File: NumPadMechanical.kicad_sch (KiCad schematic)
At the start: 35 parts, among them SW1 Push_Button, SW10 Push_Button, SW11 Push_Button, SW12 Push_Button, SW13 Push_Button, SW14 Push_Button, SW15 Push_Button, SW16 Push_Button, SW17 Push_Button, SW2 Push_Button, SW3 Push_Button, SW4 Push_Button, SW5 Push_Button, SW6 Push_Button, SW7 Push_Button, SW8 Push_Button, SW9 Push_Button, U1 STM32F103C8Tx

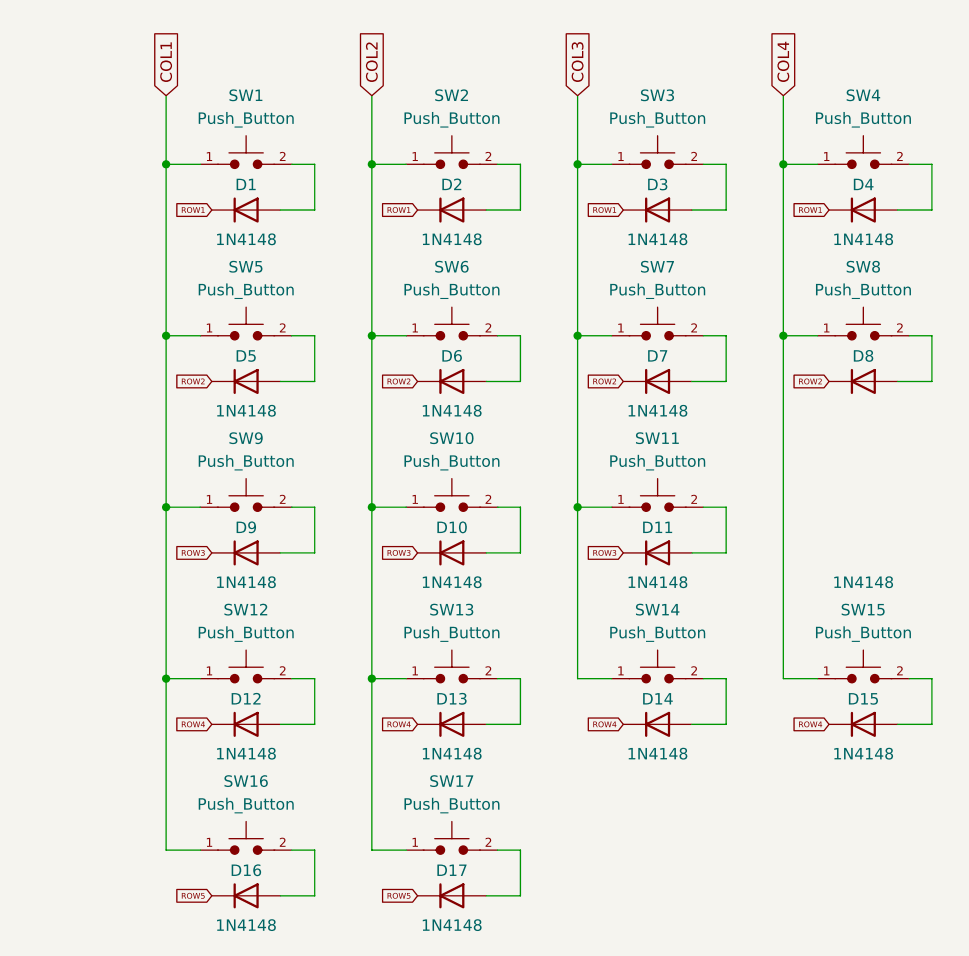
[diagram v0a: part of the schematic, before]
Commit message: Se agrega la matriz de switches al esquematico
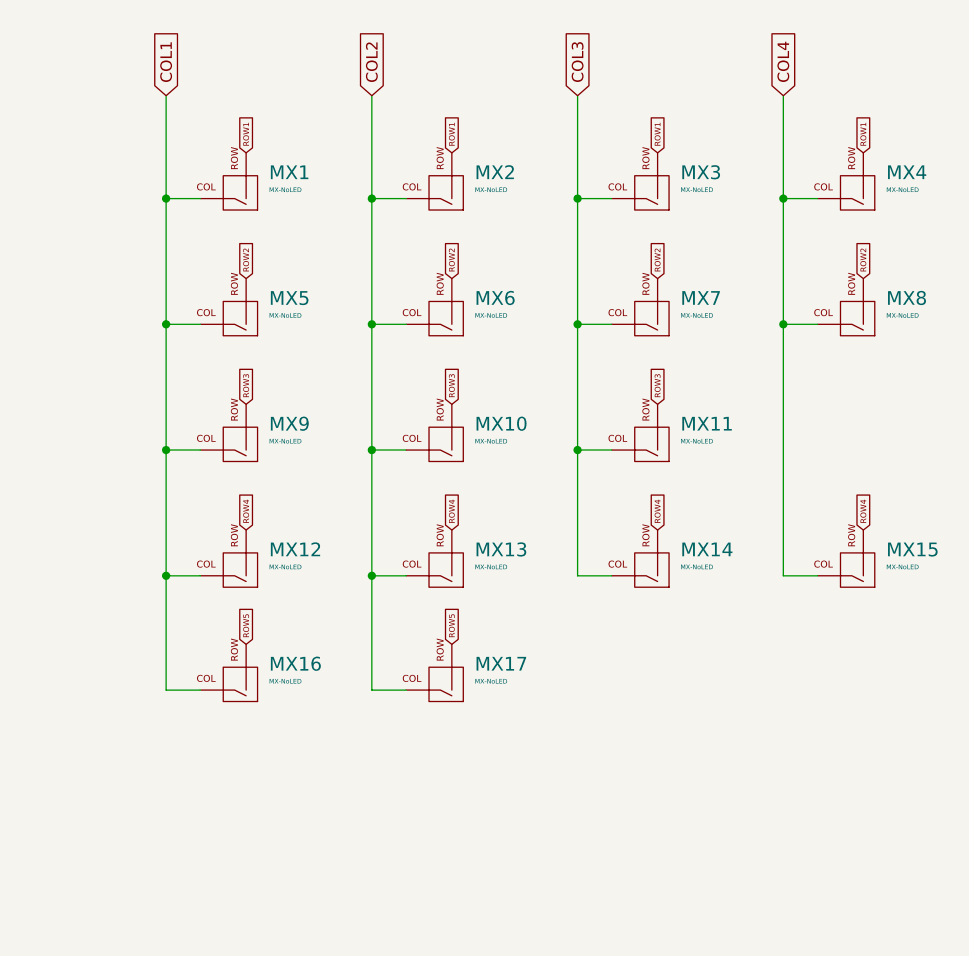
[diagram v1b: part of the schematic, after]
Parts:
- removed D1, D10, D11, D12, D13, D14, D15, D16, D17, D2, D3, D4, D5, D6, D7, D8, D9: 1N4148, Diode_THT:D_DO-35_SOD27_P7.62mm_Horizontal, symbol Diode:1N4148
- removed SW1, SW10, SW11, SW12, SW13, SW14, SW15, SW16, SW17, SW2, SW3, SW4, SW5, SW6, SW7, SW8, SW9: Push_Button, Button_Switch_THT:SW_PUSH_6mm, symbol PCM_SL_Devices:Push_Button
- added MX1, MX10, MX11, MX12, MX13, MX14, MX15, MX16, MX17, MX2, MX3, MX4, MX5, MX6, MX7, MX8, MX9: MX-NoLED, symbol MX_Alps_Hybrid:MX-NoLED
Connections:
- net COL1: now also MX1.1 (COL), MX12.1 (COL), MX16.1 (COL), MX5.1 (COL), MX9.1 (COL)
- net COL2: now also MX10.1 (COL), MX13.1 (COL), MX17.1 (COL), MX2.1 (COL), MX6.1 (COL)
- net COL3: now also MX11.1 (COL), MX14.1 (COL), MX3.1 (COL), MX7.1 (COL)
- net COL4: now also MX15.1 (COL), MX4.1 (COL), MX8.1 (COL)
- net ROW1: now also MX1.2 (ROW), MX2.2 (ROW), MX3.2 (ROW), MX4.2 (ROW)
- net ROW2: now also MX5.2 (ROW), MX6.2 (ROW), MX7.2 (ROW), MX8.2 (ROW)
- net ROW3: now also MX10.2 (ROW), MX11.2 (ROW), MX9.2 (ROW)
- net ROW4: now also MX12.2 (ROW), MX13.2 (ROW), MX14.2 (ROW), MX15.2 (ROW)
- net ROW5: now also MX16.2 (ROW), MX17.2 (ROW)

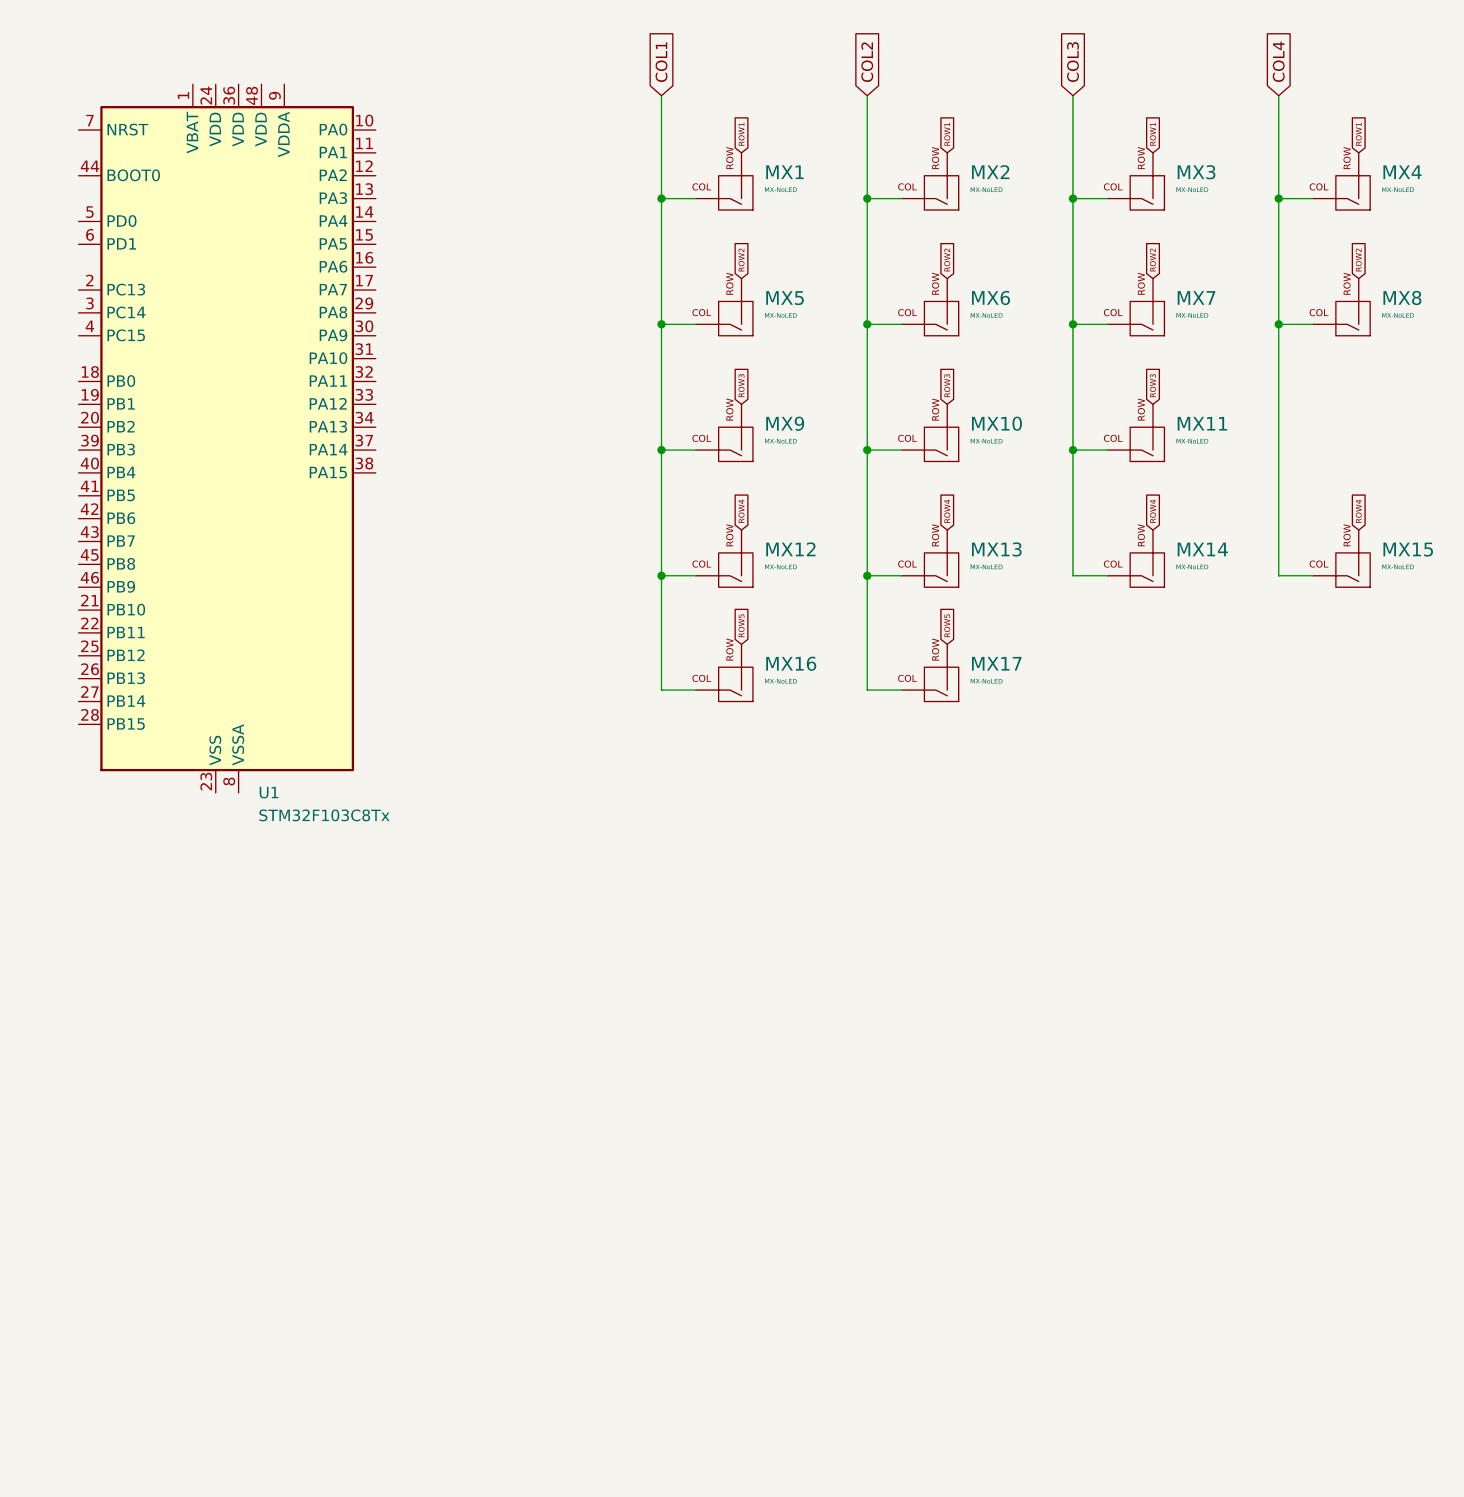
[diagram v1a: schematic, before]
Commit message: Se añaden diodos a la matriz de switches, se agrega conector usb y se coloca su cableado
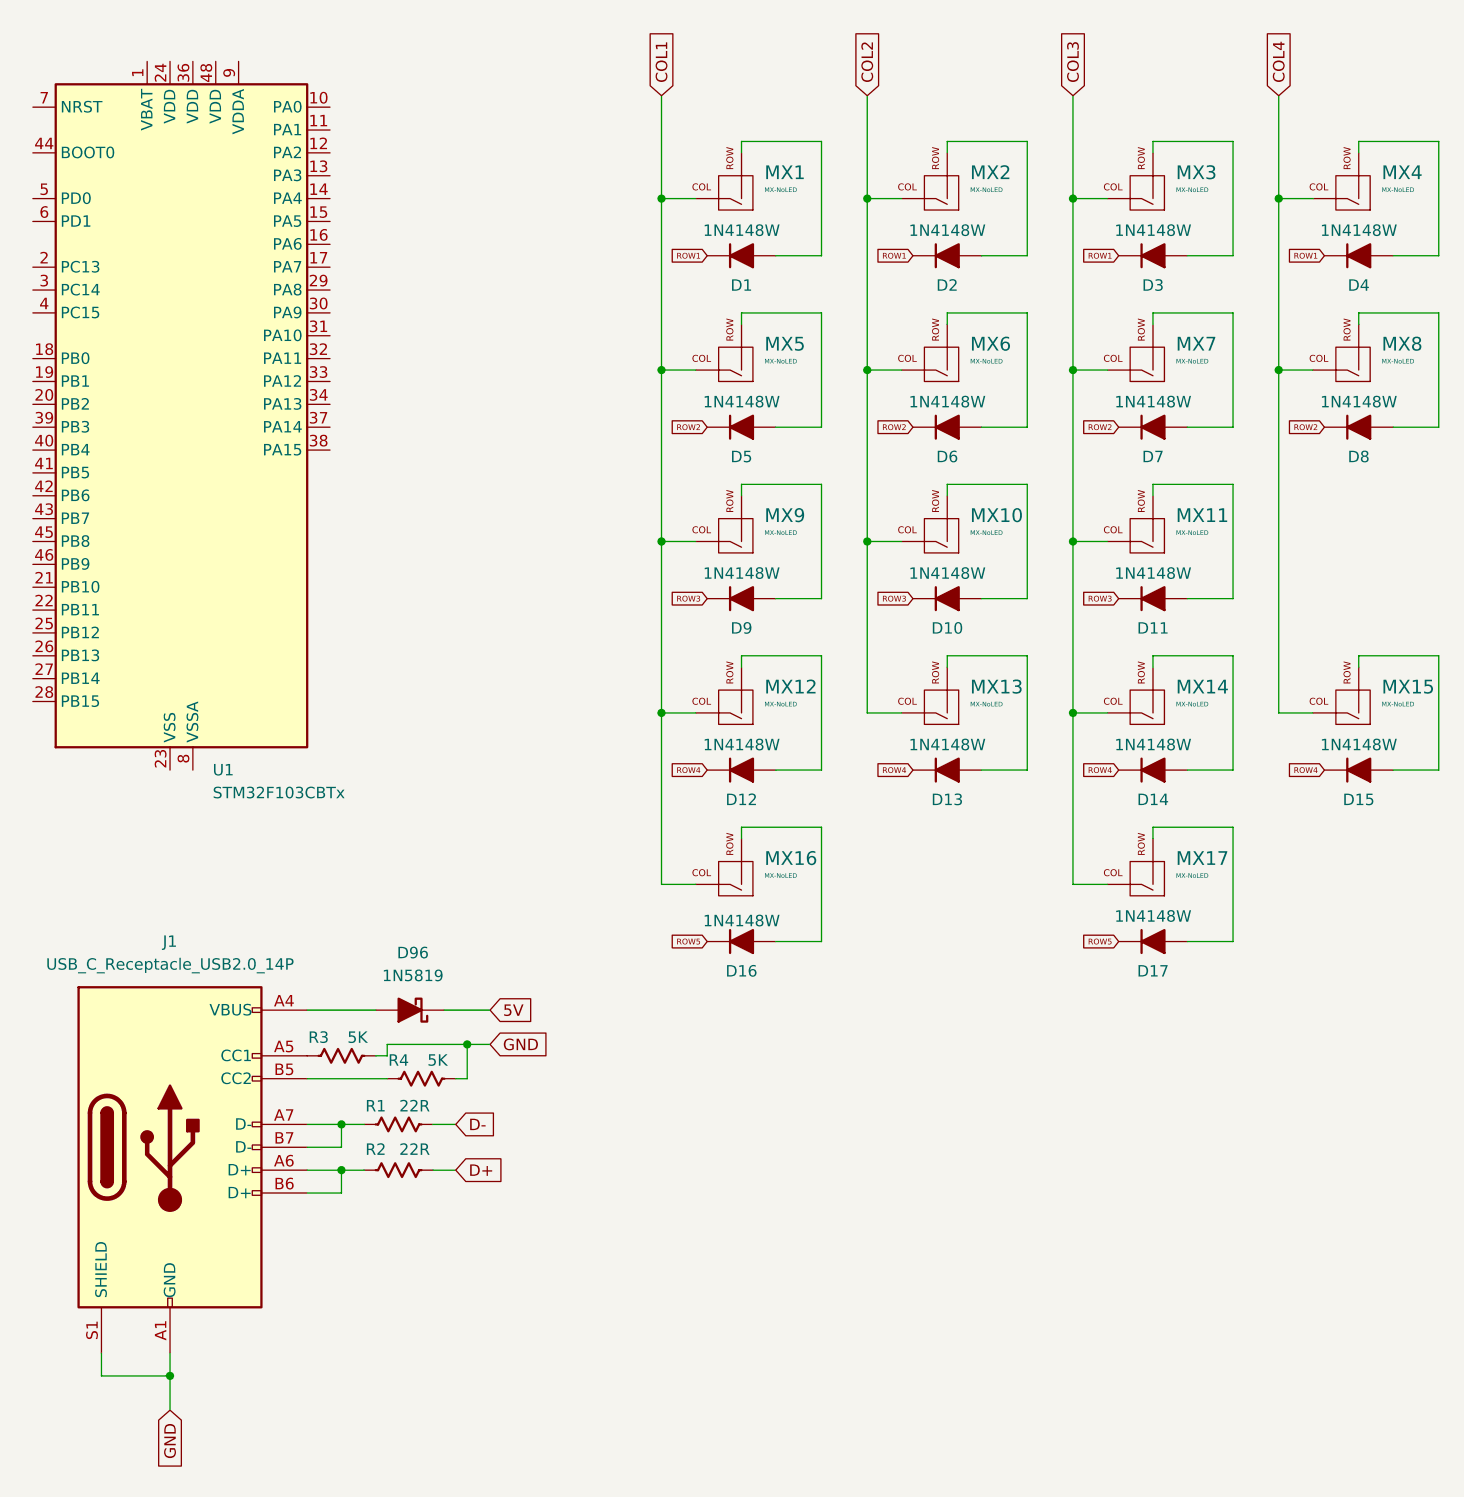
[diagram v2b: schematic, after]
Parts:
- removed U1: STM32F103C8Tx, Package_QFP:LQFP-48_7x7mm_P0.5mm, symbol MCU_ST_STM32F1:STM32F103C8Tx
- added D1, D10, D11, D12, D13, D14, D15, D16, D17, D2, D3, D4, D5, D6, D7, D8, D9: 1N4148W, Diode_SMD:D_SOD-123, symbol PCM_Diode_AKL:1N4148W
- added D96: 1N5819, Diode_SMD:D_SOD-123, symbol PCM_Diode_Schottky_AKL:D_Schottky_Generic
- added J1: USB_C_Receptacle_USB2.0_14P, Connector_USB:USB_C_Receptacle_XKB_U262-16XN-4BVC11, symbol Connector:USB_C_Receptacle_USB2.0_14P
- added R1, R2: 22R, Resistor_SMD:R_0603_1608Metric_Pad0.98x0.95mm_HandSolder, symbol PCM_Resistor_US_AKL:R_0603
- added R3, R4: 5K, Resistor_SMD:R_0603_1608Metric_Pad0.98x0.95mm_HandSolder, symbol PCM_Resistor_US_AKL:R_0603
- added U1: STM32F103CBTx, Package_QFP:LQFP-48_7x7mm_P0.5mm, symbol MCU_ST_STM32F1:STM32F103CBTx
- MX1, MX10, MX11, MX12, MX13, MX14, MX17, MX2, MX3, MX4, MX5, MX6, MX7, MX9: footprint (none) -> MX_Alps_Hybrid:MX-1U-NoLED
- MX15, MX16, MX8: footprint (none) -> MX_Alps_Hybrid:MX-2U-NoLED
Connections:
- net COL2: no longer MX17.1 (COL)
- net COL3: now also MX17.1 (COL)
- net ROW1: now also D1.1 (K), D2.1 (K), D3.1 (K), D4.1 (K); no longer MX1.2 (ROW), MX2.2 (ROW), MX3.2 (ROW), MX4.2 (ROW)
- net ROW2: now also D5.1 (K), D6.1 (K), D7.1 (K), D8.1 (K); no longer MX5.2 (ROW), MX6.2 (ROW), MX7.2 (ROW), MX8.2 (ROW)
- net ROW3: now also D10.1 (K), D11.1 (K), D9.1 (K); no longer MX10.2 (ROW), MX11.2 (ROW), MX9.2 (ROW)
- net ROW4: now also D12.1 (K), D13.1 (K), D14.1 (K), D15.1 (K); no longer MX12.2 (ROW), MX13.2 (ROW), MX14.2 (ROW), MX15.2 (ROW)
- net ROW5: now also D16.1 (K), D17.1 (K); no longer MX16.2 (ROW), MX17.2 (ROW)
- new net: D11.2 (A), MX11.2 (ROW)
- new net: D96.2 (A), J1.A4 (VBUS), J1.A9 (VBUS), J1.B4 (VBUS), J1.B9 (VBUS)
- new net: J1.A5 (CC1), R3.1
- new net: J1.A6 (D+), J1.B6 (D+), R2.1
- new net: J1.A7 (D-), J1.B7 (D-), R1.1
- new net: J1.B5 (CC2), R4.1
- new net: D13.2 (A), MX13.2 (ROW)
- new net: D17.2 (A), MX17.2 (ROW)
- new net: D12.2 (A), MX12.2 (ROW)
- new net: D15.2 (A), MX15.2 (ROW)
- new net: D16.2 (A), MX16.2 (ROW)
- new net: D9.2 (A), MX9.2 (ROW)
- new net: D3.2 (A), MX3.2 (ROW)
- new net: D1.2 (A), MX1.2 (ROW)
- new net: D2.2 (A), MX2.2 (ROW)
- new net: D8.2 (A), MX8.2 (ROW)
- new net: U1.23 (VSS), U1.35 (VSS), U1.47 (VSS)
- new net: D10.2 (A), MX10.2 (ROW)
- new net: D7.2 (A), MX7.2 (ROW)
- new net: D14.2 (A), MX14.2 (ROW)
- new net: D5.2 (A), MX5.2 (ROW)
- new net: D4.2 (A), MX4.2 (ROW)
- new net: D6.2 (A), MX6.2 (ROW)
- new net 5V: D96.1 (K)
- new net D+: R2.2
- new net D-: R1.2
- new net GND: J1.A1 (GND), J1.A12 (GND), J1.B1 (GND), J1.B12 (GND), J1.S1 (SHIELD), R3.2, R4.2
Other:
- moved on the sheet: MX10, MX11, MX12, MX13, MX14, MX15, MX16, MX5, MX6, MX7, MX8, MX9

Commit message: Se modifican huellas de dispositivos y se agregan modelos 3d en algunas de las huellas
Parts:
- D1, D10, D11, D12, D13, D14, D15, D16, D17, D2, D3, D4, D5, D6, D7, D8, D9, D96: footprint Diode_SMD:D_SOD-123 -> D_SOD-123_A:D_SOD-123_A
- MX15, MX8: footprint MX_Alps_Hybrid:MX-2U-NoLED -> MX_Alps_Hybrid:MX-Alps-Hybrid-2U-Vertical
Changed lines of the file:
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@@
 			)
 		)
-		(property "Footprint" "Diode_SMD:D_SOD-123"
+		(property "Footprint" "D_SOD-123_A:D_SOD-123_A"
 			(at 129.54 97.79 0)
 			(effects
@@
 			)
 		)
-		(property "Footprint" "Diode_SMD:D_SOD-123"
+		(property "Footprint" "D_SOD-123_A:D_SOD-123_A"
 			(at 152.4 116.84 0)
 			(effects
@@
 			)
 		)
-		(property "Footprint" "Diode_SMD:D_SOD-123"
+		(property "Footprint" "D_SOD-123_A:D_SOD-123_A"
 			(at 106.68 97.79 0)
 			(effects
@@
 			)
 		)
-		(property "Footprint" "Diode_SMD:D_SOD-123"
+		(property "Footprint" "D_SOD-123_A:D_SOD-123_A"
 			(at 69.85 124.46 0)
 			(effects
@@
 			)
 		)
-		(property "Footprint" "MX_Alps_Hybrid:MX-2U-NoLED"
+		(property "Footprint" "MX_Alps_Hybrid:MX-Alps-Hybrid-2U-Vertical"
 			(at 189.865 89.535 0)
 			(effects
@@
 			)
 		)
-		(property "Footprint" "Diode_SMD:D_SOD-123"
+		(property "Footprint" "D_SOD-123_A:D_SOD-123_A"
 			(at 106.68 116.84 0)
 			(effects
@@
 			)
 		)
-		(property "Footprint" "Diode_SMD:D_SOD-123"
+		(property "Footprint" "D_SOD-123_A:D_SOD-123_A"
 			(at 106.68 78.74 0)
 			(effects
@@
 			)
 		)
-		(property "Footprint" "Diode_SMD:D_SOD-123"
+		(property "Footprint" "D_SOD-123_A:D_SOD-123_A"
 			(at 129.54 40.64 0)
 			(effects
@@
 			)
 		)
-		(property "Footprint" "Diode_SMD:D_SOD-123"
+		(property "Footprint" "D_SOD-123_A:D_SOD-123_A"
 			(at 175.26 59.69 0)
 			(effects
@@
 			)
 		)
-		(property "Footprint" "MX_Alps_Hybrid:MX-2U-NoLED"
+		(property "Footprint" "MX_Alps_Hybrid:MX-Alps-Hybrid-2U-Vertical"
 			(at 189.865 51.435 0)
 			(effects
@@
 			)
 		)
-		(property "Footprint" "Diode_SMD:D_SOD-123"
+		(property "Footprint" "D_SOD-123_A:D_SOD-123_A"
 			(at 129.54 78.74 0)
 			(effects
@@
 			)
 		)
-		(property "Footprint" "Diode_SMD:D_SOD-123"
+		(property "Footprint" "D_SOD-123_A:D_SOD-123_A"
 			(at 152.4 40.64 0)
 			(effects
@@
 			)
 		)
-		(property "Footprint" "Diode_SMD:D_SOD-123"
+		(property "Footprint" "D_SOD-123_A:D_SOD-123_A"
 			(at 106.68 40.64 0)
 			(effects
@@
 			)
 		)
-		(property "Footprint" "Diode_SMD:D_SOD-123"
+		(property "Footprint" "D_SOD-123_A:D_SOD-123_A"
 			(at 152.4 97.79 0)
 			(effects
@@
 			)
 		)
-		(property "Footprint" "Diode_SMD:D_SOD-123"
+		(property "Footprint" "D_SOD-123_A:D_SOD-123_A"
 			(at 152.4 59.69 0)
 			(effects
@@
 			)
 		)
-		(property "Footprint" "Diode_SMD:D_SOD-123"
+		(property "Footprint" "D_SOD-123_A:D_SOD-123_A"
 			(at 106.68 59.69 0)
 			(effects
@@
 			)
 		)
-		(property "Footprint" "Diode_SMD:D_SOD-123"
+		(property "Footprint" "D_SOD-123_A:D_SOD-123_A"
 			(at 152.4 78.74 0)
 			(effects
@@
 			)
 		)
-		(property "Footprint" "Diode_SMD:D_SOD-123"
+		(property "Footprint" "D_SOD-123_A:D_SOD-123_A"
 			(at 175.26 97.79 0)
 			(effects
@@
 			)
 		)
-		(property "Footprint" "Diode_SMD:D_SOD-123"
+		(property "Footprint" "D_SOD-123_A:D_SOD-123_A"
 			(at 129.54 59.69 0)
 			(effects
@@
 			)
 		)
-		(property "Footprint" "Diode_SMD:D_SOD-123"
+		(property "Footprint" "D_SOD-123_A:D_SOD-123_A"
 			(at 175.26 40.64 0)
 			(effects

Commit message: Agregados capacitores de acoplamiento y regulador de 3v3
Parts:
- added C1, C2: 1uF, Capacitor_SMD:CP_Elec_6.3x7.7, symbol PCM_Capacitor_AKL:CP_SMD_D6.3mm_H7.7mm
- added C10, C7, C9: 10uF, symbol PCM_Elektuur:C-polar
- added C3, C4, C5, C6: 100nF, symbol PCM_Elektuur:C
- added C8: 10nF, symbol PCM_Elektuur:C
- added D18: SK6812MINI-E, kicad-keyboard-parts:MX_SK6812MINI-E, symbol kicad-keyboard-parts:SK6812MINI-E
- added FB1: FerriteBead, symbol Device:FerriteBead
- added U2: AMS1117-3.3, Package_TO_SOT_SMD:SOT-223-3_TabPin2, symbol Regulator_Linear:AMS1117-3.3
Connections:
- net 5V: now also C1.1, U2.3 (VI); no longer D96.1 (K)
- net GND: now also U1.23 (VSS), U1.35 (VSS), U1.47 (VSS), U1.8 (VSSA), C1.2, C2.2, C3.2 (-), C4.2 (-), C5.2 (-), C6.2 (-), C7.2 (-), C8.2 (-), C9.2 (-), U2.1 (GND)
- net +3.3V: now reaches U1.1 (VBAT)
- net +3.3V: now also U1.24 (VDD), U1.36 (VDD), U1.48 (VDD), C10.1 (+), C3.1 (+), C4.1 (+), C5.1 (+), C6.1 (+), C7.1 (+), FB1.2
- net +3.3VA: now reaches U1.9 (VDDA)
- net +3.3VA: now also C8.1 (+), C9.1 (+), FB1.1
- new net +5V: D96.1 (K)
- new net 3V3: C2.1, U2.2 (VO)
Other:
- title: Numpad Homemade -> Numpad Mechanical
- moved on the sheet: D1, D10, D11, D12, D13, D14, D15, D16, D17, D2, D3, D4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

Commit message: Añadido gitignore y modificaciones en el esquematico
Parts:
- FB1: value FerriteBead -> 130R
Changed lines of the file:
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@@
 			)
 		)
-		(property "Value" "FerriteBead"
+		(property "Value" "130R"
 			(at 139.6492 15.24 90)
 			(effects
